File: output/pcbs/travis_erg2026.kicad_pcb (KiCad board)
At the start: 2 copper layers, 164.1 x 160.3 mm, 176 parts

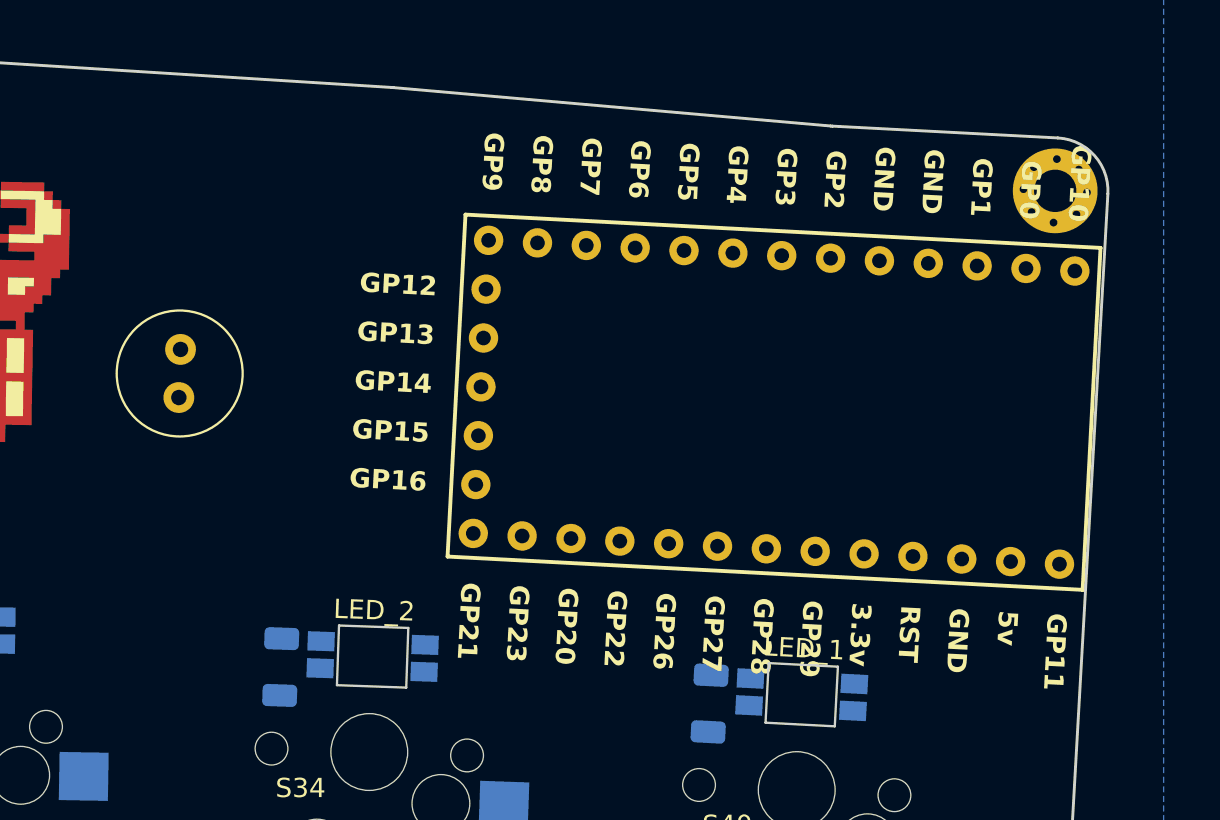
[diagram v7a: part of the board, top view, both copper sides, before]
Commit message: adjusted to fit
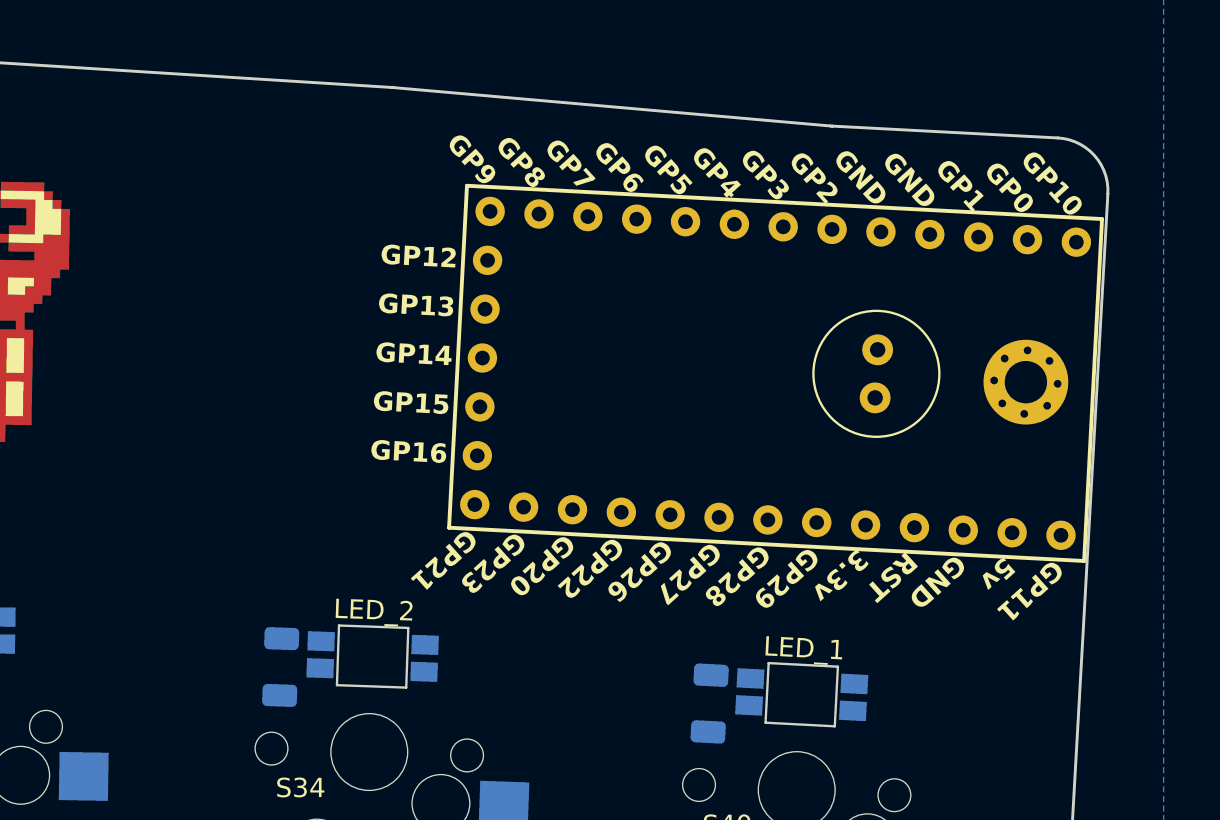
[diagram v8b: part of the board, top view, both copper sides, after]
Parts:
- moved C1 36.2 mm to (180.0, 73.7), turned to 87 degrees
- moved HOLE2 10.0 mm to (187.8, 72.9)
- moved MCU1 1.50 mm to (173.6, 72.3)
